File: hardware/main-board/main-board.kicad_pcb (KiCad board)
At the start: 4 copper layers, 105 x 38 mm, 80 parts, among them J1 USB_B_Micro, J2 DNI, J3 Display Connector, J4 Conn_01x02, SW1 SW_Push, SW2 SW_Push, SW3 SW_Push, SW4 SW_Push, SW5 SW_Detect, U1 TSL2591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

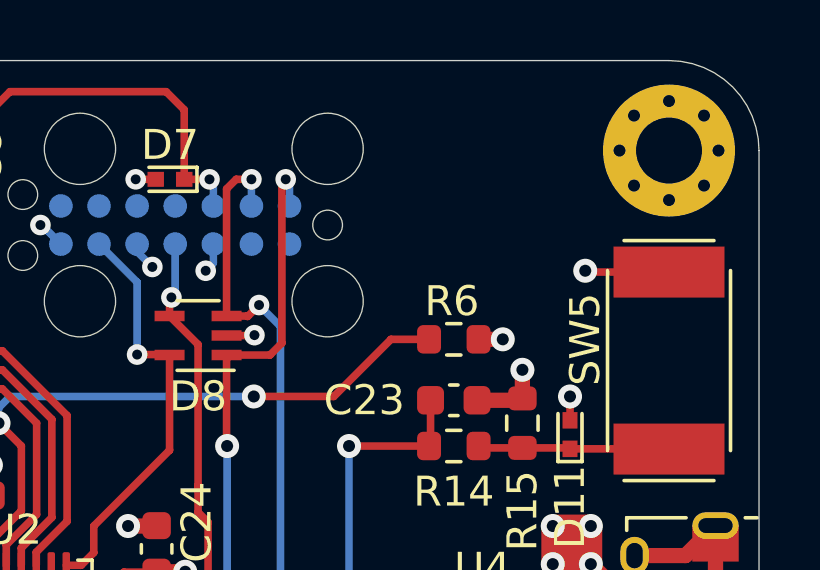
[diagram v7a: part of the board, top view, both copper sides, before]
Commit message: Add boot mode selection button
This adds a small right-angle push button, intended to be pressed via a
hole in the enclosure, to trigger the USB DFU bootloader. The current
design is pulled down with a 10k resistor normally, but pulled up to +5V
for the mode switch. There's also a 330 ohm in-line resistor like the
other buttons.

This design is subject to change, but its hard to find good references
for exactly what we're trying to do here.

Refs #11
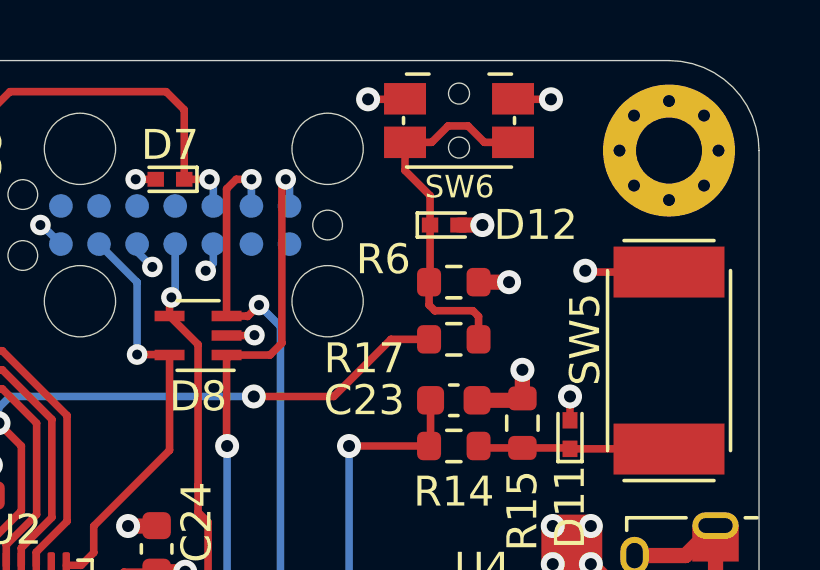
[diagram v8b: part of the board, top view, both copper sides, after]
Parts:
- added D12: ESDALC6V1-1M2, lib_fp:D_SOD-882, F.Cu at (135.5, 46.5)
- added R17: 330R, Resistor_SMD:R_0603_1608Metric, F.Cu at (135.8, 50.3)
- added SW6: SW_Boot, lib_fp:Panasonic_EVQP7C_EVQP7L, F.Cu at (136.0, 43.0)
- moved R6 1.91 mm to (135.8, 48.4)
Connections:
- R6 pad 1: /BOOT0 -> Net-(D12-Pad1)
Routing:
- net Net-(D12-Pad1): track 0.00 -> 12.8 mm
- net +3V3: track 36.2 -> 38.7 mm, vias 15 -> 17
- net GND: track 75.0 -> 76.0 mm, vias 54 -> 55
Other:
- board text added: "BOOT0"
- board text removed: "Space reserved for BOOT0 select switch"
